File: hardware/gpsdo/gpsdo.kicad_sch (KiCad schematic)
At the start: 27 parts, among them U1 74HC4040D_652, U2 74HC4040D_652, U6 REF5040AD, U7 OPA197xD

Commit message: update hardware
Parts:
- added R4: 100, Resistor_SMD:R_0201_0603Metric_Pad0.64x0.40mm_HandSolder, symbol Device:R_US
- added TP1, TP2, TP3: TestPoint, symbol Connector:TestPoint
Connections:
- net GNDA is gone; now on net GND: AD5541A.3 (AGND), C16.2, C8.2
- net DAC_Vref: now also TP2.1
- net OCXO_625KHZ: now also TP3.1
- net OCXO_Vref: now also R4.1; no longer C6.1, C7.1, OSC5A2B1.3 (Vref)
- new net: C6.1, C7.1, OSC5A2B1.3 (Vref), R4.2, TP1.1
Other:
- note added: "Grounding"
- moved on the sheet: AD5541A, C1, C10, C11, C12, C13, C14, C16, C4, C5, C6, C7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

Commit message: update pcb; update hal
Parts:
- added R2: 1.1k, Resistor_SMD:R_0201_0603Metric_Pad0.64x0.40mm_HandSolder, symbol Device:R_US
- added R3: 2.2k, Resistor_SMD:R_0201_0603Metric_Pad0.64x0.40mm_HandSolder, symbol Device:R_US
- TP1: footprint (none) -> TestPoint:TestPoint_Pad_D1.5mm
- TP2: renamed from TP3; footprint (none) -> TestPoint:TestPoint_Pad_D1.5mm
- TP3: renamed from TP2; footprint (none) -> TestPoint:TestPoint_Pad_D1.5mm
- U4: renamed from AD5541A; value ~ -> AD5541A; footprint (none) -> Package_SO:MSOP-10_3x3mm_P0.5mm
- renumbered C2 to C1, C5 to C10, C4 to C11, C11 to C12, C12 to C13, C13 to C14, C14 to C15, C3 to C2, C6 to C3, C7 to C4, C1 to C5, C10 to C6, C8 to C7, C9 to C8, C16 to C9, R4 to R1, R7 to R4, R2 to R5, R3 to R6, R1 to R7, U6 to U3, U7 to U5
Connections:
- net GND: now also R3.2
- net OCXO_Out: now also R2.2; no longer U1.10 (~CP)
- net VCC_3.3V: now also C1.1, C2.1, U1.16 (VCC), U2.16 (VCC)
- net VCC_5V: no longer C1.1, C2.1, U1.16 (VCC), U2.16 (VCC)
- new net: R2.1, R3.1, U1.10 (~CP)
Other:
- added sheet Microcontroller (Microcontroller.kicad_sch)
- note added: "Counting"
- moved on the sheet: C1, C2, TP2, U1, U2

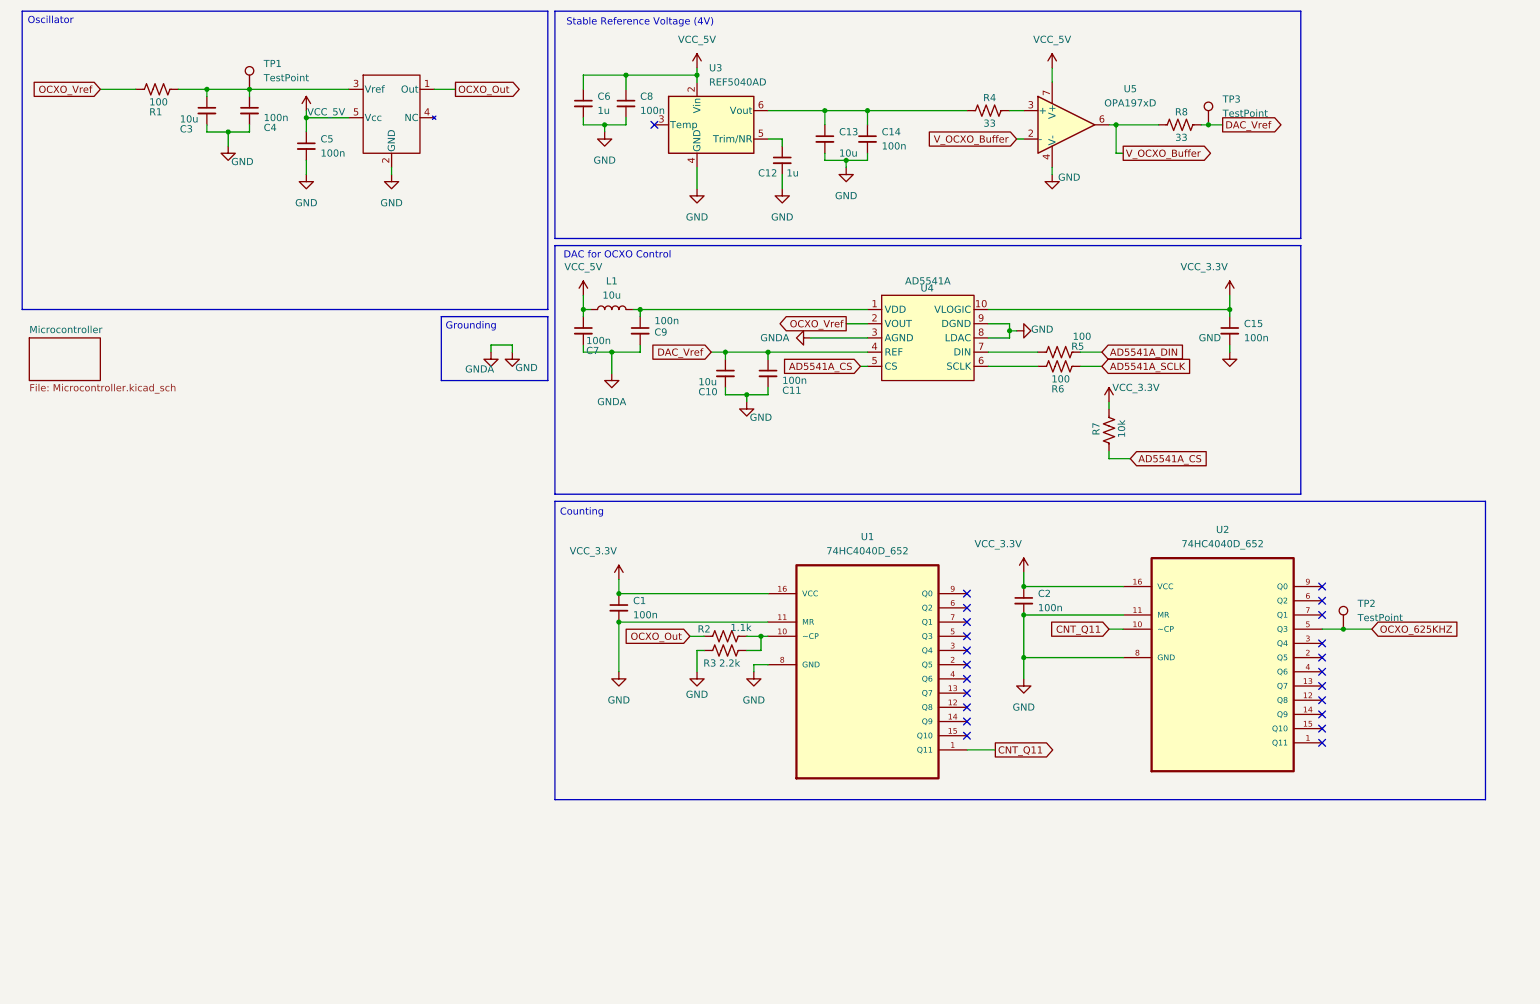
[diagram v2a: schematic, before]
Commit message: update hal; update schematics and routing
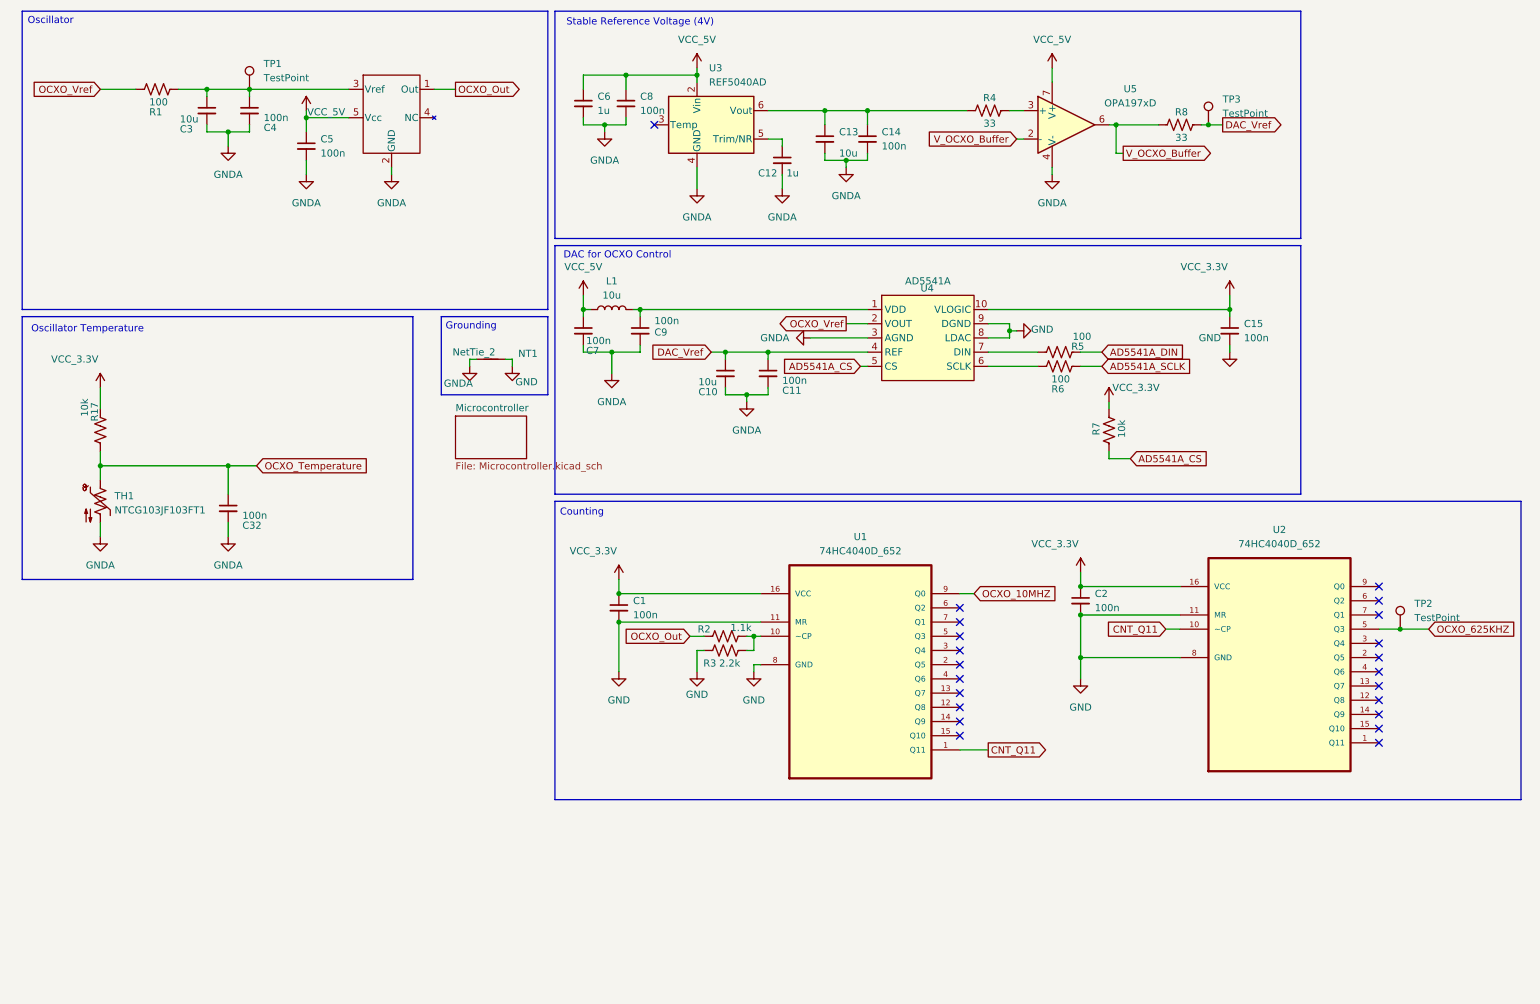
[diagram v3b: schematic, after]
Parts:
- added C32: 100n, Capacitor_SMD:C_0201_0603Metric_Pad0.64x0.40mm_HandSolder, symbol Device:C_Small
- added NT1: NetTie_2, NetTie:NetTie-2_THT_Pad0.3mm, symbol Device:NetTie_2
- added R17: 10k, Resistor_SMD:R_0201_0603Metric_Pad0.64x0.40mm_HandSolder, symbol Device:R_US
- added TH1: NTCG103JF103FT1, Resistor_SMD:R_0402_1005Metric_Pad0.72x0.64mm_HandSolder, symbol Device:Thermistor_NTC_US
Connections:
- net GND: now also NT1.2; no longer C10.2, C11.2, C12.2, C13.2, C14.2, C3.2, C4.2, C5.2, C6.2, C7.2, C8.2, C9.2, OSC5A2B1.2 (GND), U3.4 (GND), U4.3 (AGND), U5.4 (V-)
- net VCC_3.3V: now also R17.2
- net OCXO_10MHZ: now reaches U1.9 (Q0)
- new net GNDA: C10.2, C11.2, C12.2, C13.2, C14.2, C3.2, C32.2, C4.2, C5.2, C6.2, C7.2, C8.2, C9.2, NT1.1, OSC5A2B1.2 (GND), TH1.2, U3.4 (GND), U4.3 (AGND), U5.4 (V-)
- new net OCXO_Temperature: C32.1, R17.1, TH1.1
- no-connect marks 23 -> 22
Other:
- note added: "Oscillator Temperature"
- moved on the sheet: C2, TP2, U1, U2

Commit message: update routing
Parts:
- removed TP2: TestPoint, TestPoint:TestPoint_Pad_D1.5mm, symbol Connector:TestPoint
- added NT3: NetTie_2, NetTie:NetTie-2_THT_Pad0.3mm, symbol Device:NetTie_2
- U1, U2: JLC (none) -> C27387
- U3: JLC (none) -> C1575304
- U4: JLC (none) -> C578210
- U5: JLC (none) -> C79274
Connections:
- net GND: now also NT3.2
- net GNDA: now also NT3.1
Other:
- moved on the sheet: NT1

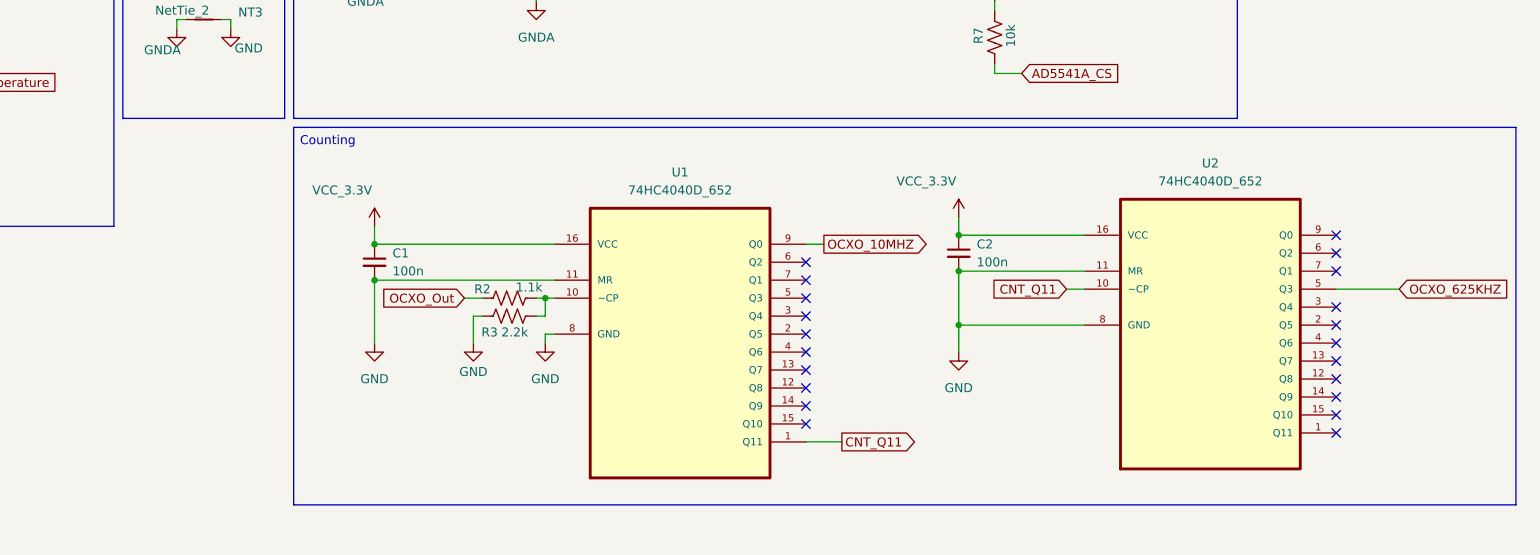
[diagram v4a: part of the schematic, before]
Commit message: update routing; bugfix in downsampling; replace voltage dividers with level shifter
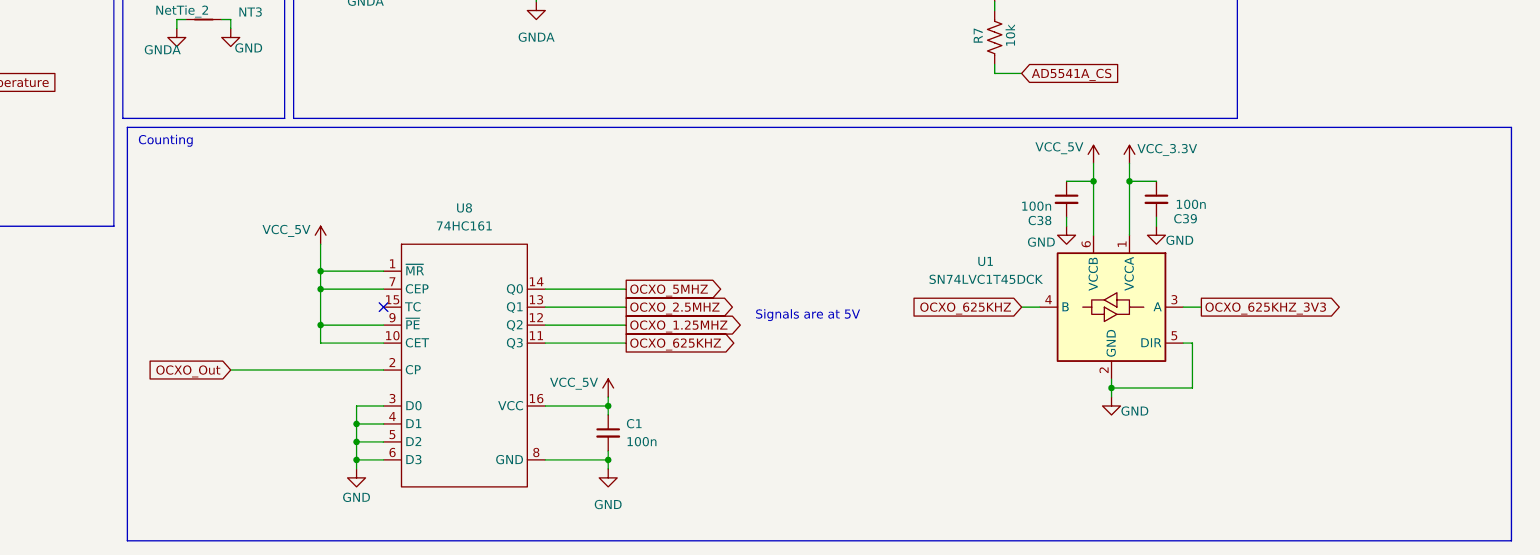
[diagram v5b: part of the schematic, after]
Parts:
- removed C2: 100n, Capacitor_SMD:C_0201_0603Metric_Pad0.64x0.40mm_HandSolder, symbol Device:C_Small
- removed R2: 1.1k, Resistor_SMD:R_0201_0603Metric_Pad0.64x0.40mm_HandSolder, symbol Device:R_US
- removed R3: 2.2k, Resistor_SMD:R_0201_0603Metric_Pad0.64x0.40mm_HandSolder, symbol Device:R_US
- removed U1, U2: 74HC4040D_652, nexperia:SOIC127P600X175-16N, symbol 74HC4040D_652:74HC4040D_652
- added C38, C39: 100n, Capacitor_SMD:C_0201_0603Metric_Pad0.64x0.40mm_HandSolder, symbol Device:C_Small
- added U1: SN74LVC1T45DCK, Package_TO_SOT_SMD:SOT-363_SC-70-6, symbol Logic_LevelTranslator:SN74LVC1T45DCK
- added U8: 74HC161, Package_SO:SO-16_3.9x9.9mm_P1.27mm, symbol nexperia:74HC161
- C1, C11, C14, C15, C32, C4, C5, C7, C8, C9: JLC (none) -> C14663; Package (none) -> 0603
- C10, C13, C3, L1: JLC (none) -> C19702; Package (none) -> 0603
- C12, C6: JLC (none) -> C15849; Package (none) -> 0603
- OSC5A2B1, TP1, TP3: now left out of the parts list
- R1, R5, R6: JLC (none) -> C22775; Package (none) -> 0603
- R17, R7: JLC (none) -> C25804; Package (none) -> 0603
- R4, R8: JLC (none) -> C23140; Package (none) -> 0603
- TH1: footprint Resistor_SMD:R_0402_1005Metric_Pad0.72x0.64mm_HandSolder -> Capacitor_SMD:C_01005_0402Metric_Pad0.57x0.30mm_HandSolder; Package (none) -> 1005
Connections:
- net GND: now also C38.2, C39.2, U1.2 (GND), U1.5 (DIR), U8.3 (D0), U8.4 (D1), U8.5 (D2), U8.6 (D3), U8.8 (GND)
- net OCXO_625KHZ: now also U1.4 (B), U8.11 (Q3)
- net OCXO_Out: now also U8.2 (CP)
- net VCC_3.3V: now also C39.1, U1.1 (VCCA); no longer C1.1
- net VCC_5V: now also C1.1, C38.1, U1.6 (VCCB), U8.1 (~{MR}), U8.10 (CET), U8.16 (VCC), U8.7 (CEP), U8.9 (~{PE})
- new net OCXO_1.25MHZ: U8.12 (Q2)
- new net OCXO_2.5MHZ: U8.13 (Q1)
- new net OCXO_5MHZ: U8.14 (Q0)
- new net OCXO_625KHZ_3V3: U1.3 (A)
- no-connect marks 22 -> 2
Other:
- note added: "Signals are at 5V"
- moved on the sheet: C1

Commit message: bugfix in bom
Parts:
- L1: JLC C19702 -> C1035
- U1: JLC (none) -> C9382
- U8: JLC (none) -> C22436995

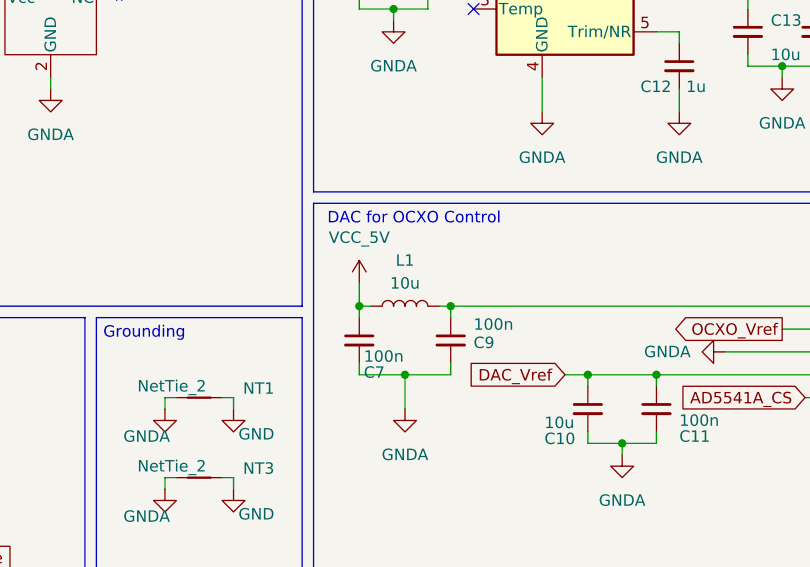
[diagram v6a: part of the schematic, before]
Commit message: version 1 put into production
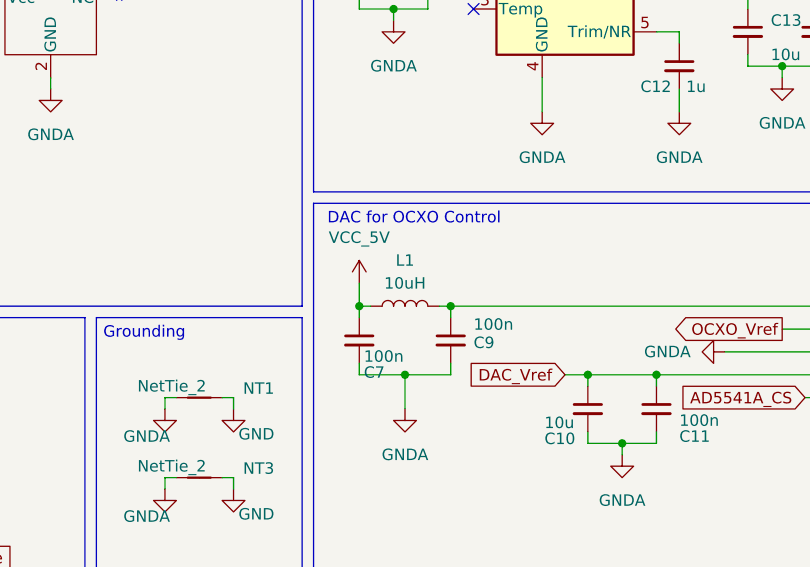
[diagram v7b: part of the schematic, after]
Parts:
- L1: value 10u -> 10uH
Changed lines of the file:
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@@
 			)
 		)
-		(property "Value" "10u"
+		(property "Value" "10uH"
 			(at 120.65 66.04 90)
 			(effects

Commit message: revisit footprints
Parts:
- C1, C10, C11, C12, C13, C14, C15, C3, C32, C38, C39, C4, C5, C6, C7, C8, C9: footprint Capacitor_SMD:C_0201_0603Metric_Pad0.64x0.40mm_HandSolder -> Capacitor_SMD:C_0603_1608Metric
- L1: footprint Capacitor_SMD:C_0201_0603Metric_Pad0.64x0.40mm_HandSolder -> Inductor_SMD:L_0603_1608Metric
- R1, R17, R4, R5, R6, R7, R8: footprint Resistor_SMD:R_0201_0603Metric_Pad0.64x0.40mm_HandSolder -> Resistor_SMD:R_0603_1608Metric
- TH1: footprint Capacitor_SMD:C_01005_0402Metric_Pad0.57x0.30mm_HandSolder -> Resistor_SMD:R_0603_1608Metric; Package 1005 -> 0603
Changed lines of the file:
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@@
 			)
 		)
-		(property "Footprint" "Capacitor_SMD:C_0201_0603Metric_Pad0.64x0.40mm_HandSolder"
+		(property "Footprint" "Capacitor_SMD:C_0603_1608Metric"
 			(at 140.97 80.01 0)
 			(effects
@@
 			)
 		)
-		(property "Footprint" "Capacitor_SMD:C_0201_0603Metric_Pad0.64x0.40mm_HandSolder"
+		(property "Footprint" "Capacitor_SMD:C_0603_1608Metric"
 			(at 158.75 38.1 0)
 			(effects
@@
 			)
 		)
-		(property "Footprint" "Resistor_SMD:R_0201_0603Metric_Pad0.64x0.40mm_HandSolder"
+		(property "Footprint" "Resistor_SMD:R_0603_1608Metric"
 			(at 188.214 32.004 90)
 			(effects
@@
 			)
 		)
-		(property "Footprint" "Capacitor_SMD:C_0201_0603Metric_Pad0.64x0.40mm_HandSolder"
+		(property "Footprint" "Capacitor_SMD:C_0603_1608Metric"
 			(at 232.41 113.03 0)
 			(effects
@@
 			)
 		)
-		(property "Footprint" "Resistor_SMD:R_0201_0603Metric_Pad0.64x0.40mm_HandSolder"
+		(property "Footprint" "Resistor_SMD:R_0603_1608Metric"
 			(at 200.914 77.724 90)
 			(effects
@@
 			)
 		)
-		(property "Footprint" "Resistor_SMD:R_0201_0603Metric_Pad0.64x0.40mm_HandSolder"
+		(property "Footprint" "Resistor_SMD:R_0603_1608Metric"
 			(at 208.534 89.916 90)
 			(effects
@@
 			)
 		)
-		(property "Footprint" "Capacitor_SMD:C_0201_0603Metric_Pad0.64x0.40mm_HandSolder"
+		(property "Footprint" "Capacitor_SMD:C_0603_1608Metric"
 			(at 123.19 31.75 0)
 			(effects
@@
 			)
 		)
-		(property "Footprint" "Capacitor_SMD:C_0201_0603Metric_Pad0.64x0.40mm_HandSolder"
+		(property "Footprint" "Capacitor_SMD:C_0603_1608Metric"
 			(at 66.04 39.37 0)
 			(effects
@@
 			)
 		)
-		(property "Footprint" "Resistor_SMD:R_0201_0603Metric_Pad0.64x0.40mm_HandSolder"
+		(property "Footprint" "Resistor_SMD:R_0603_1608Metric"
 			(at 200.914 75.184 90)
 			(effects
@@
 			)
 		)
-		(property "Footprint" "Resistor_SMD:R_0201_0603Metric_Pad0.64x0.40mm_HandSolder"
+		(property "Footprint" "Resistor_SMD:R_0603_1608Metric"
 			(at 39.624 28.194 90)
 			(effects
@@
 			)
 		)
-		(property "Footprint" "Capacitor_SMD:C_01005_0402Metric_Pad0.57x0.30mm_HandSolder"
+		(property "Footprint" "Resistor_SMD:R_0603_1608Metric"
 			(at 29.21 101.6 0)
 			(effects
@@
 			)
 		)
-		(property "Package" "1005"
+		(property "Package" "0603"
 			(at 29.21 102.87 0)
 			(effects
@@
 			)
 		)
-		(property "Footprint" "Capacitor_SMD:C_0201_0603Metric_Pad0.64x0.40mm_HandSolder"
+		(property "Footprint" "Capacitor_SMD:C_0603_1608Metric"
 			(at 115.57 72.39 0)
 			(effects
@@
 			)
 		)
-		(property "Footprint" "Capacitor_SMD:C_0201_0603Metric_Pad0.64x0.40mm_HandSolder"
+		(property "Footprint" "Capacitor_SMD:C_0603_1608Metric"
 			(at 55.88 33.02 0)
 			(effects
@@
 			)
 		)
-		(property "Footprint" "Capacitor_SMD:C_0201_0603Metric_Pad0.64x0.40mm_HandSolder"
+		(property "Footprint" "Capacitor_SMD:C_0603_1608Metric"
 			(at 48.26 33.02 0)
 			(effects
@@
 			)
 		)
-		(property "Footprint" "Capacitor_SMD:C_0201_0603Metric_Pad0.64x0.40mm_HandSolder"
+		(property "Footprint" "Capacitor_SMD:C_0603_1608Metric"
 			(at 219.71 113.03 0)
 			(effects
@@
 			)
 		)
-		(property "Footprint" "Capacitor_SMD:C_0201_0603Metric_Pad0.64x0.40mm_HandSolder"
+		(property "Footprint" "Capacitor_SMD:C_0603_1608Metric"
 			(at 115.57 31.75 0)
 			(effects
@@
 			)
 		)
-		(property "Footprint" "Capacitor_SMD:C_0201_0603Metric_Pad0.64x0.40mm_HandSolder"
+		(property "Footprint" "Capacitor_SMD:C_0603_1608Metric"
 			(at 166.37 38.1 0)
 			(effects
@@
 			)
 		)
-		(property "Footprint" "Resistor_SMD:R_0201_0603Metric_Pad0.64x0.40mm_HandSolder"
+		(property "Footprint" "Resistor_SMD:R_0603_1608Metric"
 			(at 28.194 89.916 90)
 			(effects
@@
 			)
 		)
-		(property "Footprint" "Capacitor_SMD:C_0201_0603Metric_Pad0.64x0.40mm_HandSolder"
+		(property "Footprint" "Capacitor_SMD:C_0603_1608Metric"
 			(at 148.59 80.01 0)
 			(effects
@@
 			)
 		)
-		(property "Footprint" "Capacitor_SMD:C_0201_0603Metric_Pad0.64x0.40mm_HandSolder"
+		(property "Footprint" "Capacitor_SMD:C_0603_1608Metric"
 			(at 231.14 72.39 0)
 			(effects
@@
 			)
 		)
-		(property "Footprint" "Resistor_SMD:R_0201_0603Metric_Pad0.64x0.40mm_HandSolder"
+		(property "Footprint" "Resistor_SMD:R_0603_1608Metric"
 			(at 222.504 34.544 90)
 			(effects
@@
 			)
 		)
-		(property "Footprint" "Capacitor_SMD:C_0201_0603Metric_Pad0.64x0.40mm_HandSolder"
+		(property "Footprint" "Inductor_SMD:L_0603_1608Metric"
 			(at 120.65 68.58 0)
 			(effects
@@
 			)
 		)
-		(property "Footprint" "Capacitor_SMD:C_0201_0603Metric_Pad0.64x0.40mm_HandSolder"
+		(property "Footprint" "Capacitor_SMD:C_0603_1608Metric"
 			(at 154.94 146.05 0)
 			(effects
@@
 			)
 		)
-		(property "Footprint" "Capacitor_SMD:C_0201_0603Metric_Pad0.64x0.40mm_HandSolder"
+		(property "Footprint" "Capacitor_SMD:C_0603_1608Metric"
 			(at 151.13 41.91 0)
 			(effects
@@
 			)
 		)
-		(property "Footprint" "Capacitor_SMD:C_0201_0603Metric_Pad0.64x0.40mm_HandSolder"
+		(property "Footprint" "Capacitor_SMD:C_0603_1608Metric"
 			(at 52.07 104.14 0)
 			(effects
@@
 			)
 		)
-		(property "Footprint" "Capacitor_SMD:C_0201_0603Metric_Pad0.64x0.40mm_HandSolder"
+		(property "Footprint" "Capacitor_SMD:C_0603_1608Metric"
 			(at 125.73 72.39 0)
 			(effects
